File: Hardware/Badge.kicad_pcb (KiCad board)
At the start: 2 copper layers, 100 x 100 mm, 118 parts, among them J1 Battery_Conn, J2 Conn_01x02, J3 DEBUG, J4 Conn_02x15_Counter_Clockwise, J5 Conn_01x12, P1 USB_C_Plug_USB2.0, Q1 SI1967DH-T1-GE3, Q2 2SC4213, SW1 BOOT_MODE, SW2 RESET, SW3 PWR_BATT, SW4 SEL_BATT, SW5 Button B, SW6 Button A, U1 W25Q128JVS, U2 MCP73832-2-OT, U3 LD1117S33TR_SOT223, U4 RP2040, U5 BHI160B, U6 BMM150, U7 ESP32-S3-WROOM-1, X1 Simple_Addon_v2, Y1 12MHz_GND24

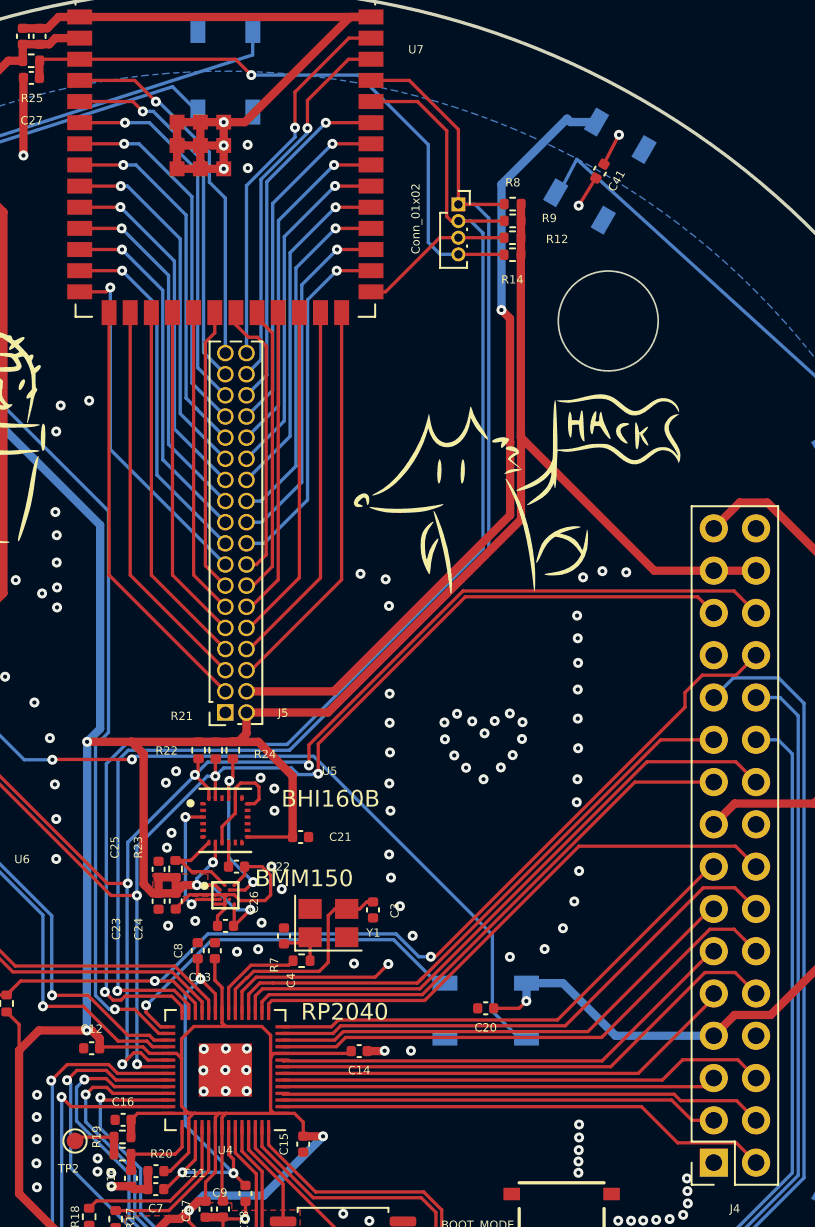
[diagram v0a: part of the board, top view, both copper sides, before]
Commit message: Inverted TX/RX from ESP32 - added INT line from BHI - Changed ESP32 dbg port to bigger footprint
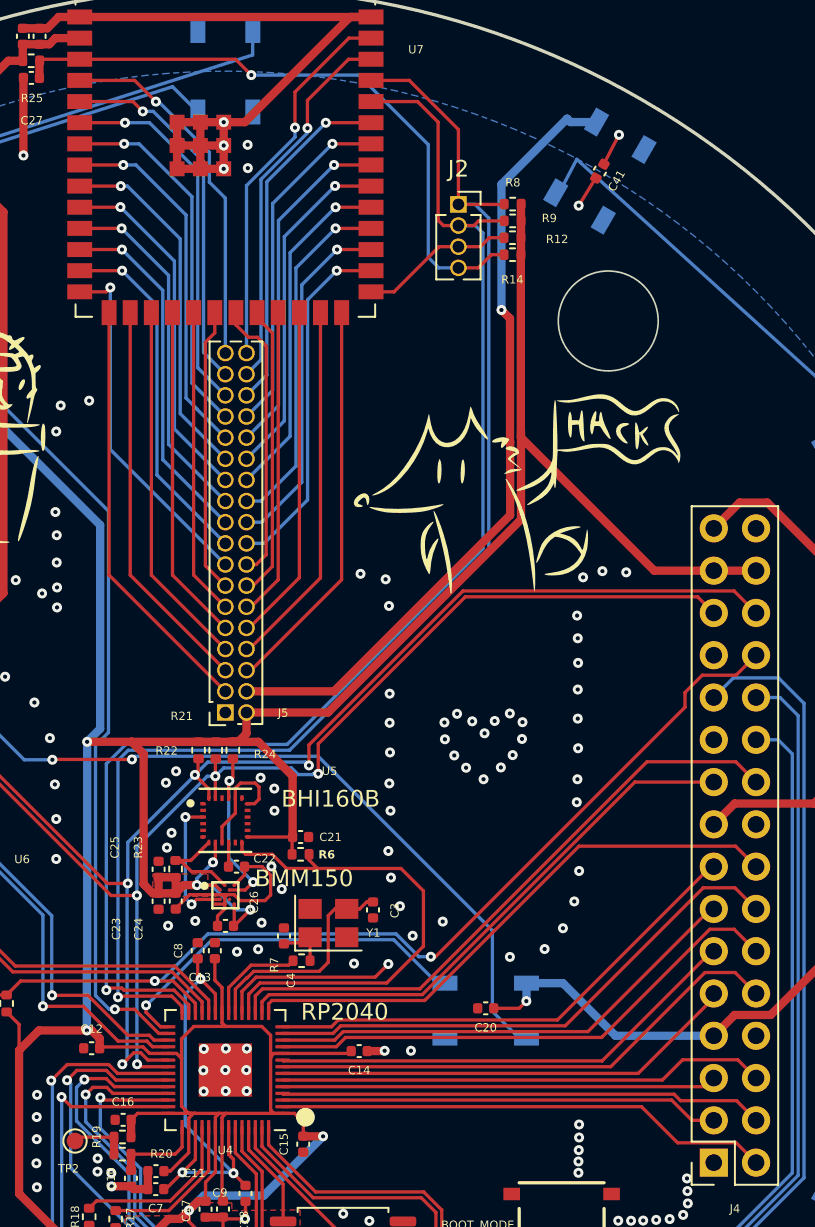
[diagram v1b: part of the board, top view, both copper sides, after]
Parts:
- added R6: 4.7k, Resistor_SMD:R_0402_1005Metric, F.Cu at (104.5, 102.0)
- J2: footprint Connector_PinSocket_1.00mm:PinSocket_1x04_P1.00mm_Vertical -> Connector_PinSocket_1.27mm:PinSocket_1x04_P1.27mm_Vertical
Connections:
- J4 pad 21: /GPIO_15 -> unconnected-(J4-Pin_21-Pad21)
- U4 pad 18: /GPIO_15 -> /INT
- U4 pad 27: /ESP_TX -> /ESP_RX
- U4 pad 28: /ESP_RX -> /ESP_TX
- U5 pad 12: /Gyros/INT -> /INT
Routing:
- net /GPIO_15: track 35.7 -> 0.00 mm
- net /INT: track 0.00 -> 29.6 mm
- net /ESP_EN: track 37.3 -> 38.5 mm
- net +3V3: track 317.6 -> 318.7 mm
- net /ESP_RX: track 82.0 -> 82.8 mm
- net GND: vias 190 -> 191

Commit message: First modification for v2
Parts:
- removed BT1: Battery_Cell, Battery:BatteryHolder_LINX_BAT-HLD-012-SMT
- removed D16: D_Schottky, Diode_SMD:D_SMA
- removed J2: Conn_01x02, Connector_PinSocket_1.27mm:PinSocket_1x04_P1.27mm_Vertical
- removed R22: 4.7k, Resistor_SMD:R_0402_1005Metric
- added C48: NC, Capacitor_SMD:C_0402_1005Metric, F.Cu at (67.6, 127.5)
- added C49: NC, Capacitor_SMD:C_0402_1005Metric, F.Cu at (67.6, 129.5)
- added C50: NC, Capacitor_SMD:C_0402_1005Metric, F.Cu at (67.6, 131.5)
- added C51: 10nF, Capacitor_SMD:C_0402_1005Metric, F.Cu at (82.7, 120.7)
- added D17: D, Diode_SMD:D_SOD-123F, F.Cu at (74.8, 125.4)
- added IC2: ST25DV04K-IER6S3, ST25DV:SOIC127P600X175-8N, F.Cu at (82.5, 124.9)
- added J6: Internal_I2C, Connector_PinHeader_1.00mm:PinHeader_1x03_P1.00mm_Vertical, F.Cu at (111.8, 97.6)
- added P2: ESP_DATA, Connector_USB:USB_C_Receptacle_Palconn_UTC16-G, F.Cu at (67.6, 70.5)
- added R29: 10k, Resistor_SMD:R_0402_1005Metric, F.Cu at (141.3, 62.3)
- added R30: 10k, Resistor_SMD:R_0402_1005Metric, F.Cu at (141.3, 64.3)
- added SW7: ESP_RST, TS-1184:TS-1187A-B-A-B, F.Cu at (130.1, 73.2)
- J3: footprint Connector_PinSocket_2.54mm:PinSocket_1x03_P2.54mm_Vertical -> Connector_PinHeader_1.27mm:PinHeader_1x03_P1.27mm_Vertical
- R12, R8, R9: value 10k -> 4.7k
- R21: value 4.7k -> 10k
- SW4: value SEL_BATT -> ESP_BOOT; footprint Button_Switch_SMD:SW_SPDT_CK-JS102011SAQN -> TS-1184:TS-1187A-B-A-B
- moved SW4 86.8 mm to (130.0, 66.2), turned to 0 degrees
- moved J1 40.8 mm to (88.7, 133.4)
- moved R12 19.3 mm to (135.4, 58.3)
- moved R14 19.3 mm to (135.4, 59.3)
- moved R9 19.3 mm to (135.4, 57.3)
- moved R8 19.3 mm to (135.4, 56.3)
- moved J3 7.20 mm to (85.4, 106.0)
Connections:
- net Net-(U5-ASCK) renamed /Gyros/INT_SCK
- net Net-(U5-ASDA) renamed /Gyros/INT_SDA
- J5 pad 15: /WiFi_BT/IO43 -> unconnected-(J5-Pin_15-Pad15)
- J5 pad 17: /WiFi_BT/IO44 -> unconnected-(J5-Pin_17-Pad17)
- R12 pad 1: /ESP_BOOT -> +3V3
- R12 pad 2: +3V3 -> /I2C_SCL
- R14 pad 1: /ESP_EN -> /ESP_RX
- R21 pad 1: +3V3 -> /ESP_TX
- R21 pad 2: /I2C_SCL -> +3V3
- R6 pad 2: /INT -> /NFC_INT
- R8 pad 1: /ESP_TX -> +3V3
- R8 pad 2: +3V3 -> /I2C_SDA
- R9 pad 1: /ESP_RX -> +3V3
- R9 pad 2: +3V3 -> /SEN_INT
- SW3 pad 1: Net-(D16-K) -> Net-(J1-Pin_2)
- SW4 pad 1: Net-(J1-Pin_2) -> GND
- SW4 pad 2: Net-(D16-A) -> /WiFi_BT/ESP_BOOT
- U2 pad 3: Net-(D16-K) -> Net-(J1-Pin_2)
- U4 pad 17: /GPIO_14 -> /NFC_INT
- U4 pad 18: /INT -> /SEN_INT
- U5 pad 12: /INT -> /SEN_INT
- U7 pad 13: /WiFi_BT/IO44 -> /WiFi_BT/ESP_USB-
- U7 pad 14: /WiFi_BT/IO43 -> /WiFi_BT/ESP_USB+
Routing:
- net (no net): track 0.00 -> 72.7 mm, vias 0 -> 2
- net Net-(D16-K): track 48.4 -> 0.00 mm
- net Net-(BT1-+): track 36.7 -> 0.00 mm
- net /INT: track 29.6 -> 0.00 mm
- net /WiFi_BT/IO44: track 21.6 -> 0.00 mm, vias 1 -> 0
- net /WiFi_BT/IO43: track 21.5 -> 0.00 mm, vias 1 -> 0
- net /ESP_RX: track 82.8 -> 72.6 mm
- net /ESP_TX: track 82.1 -> 74.9 mm
- net /SWCLK: track 22.5 -> 15.8 mm
- net /SWD: track 21.0 -> 14.8 mm
- net Net-(D16-A): track 4.22 -> 0.00 mm
- net /ESP_BOOT: track 9.34 -> 5.21 mm
- net /ESP_EN: track 38.5 -> 35.4 mm
- net Net-(J1-Pin_2): track 8.89 -> 10.7 mm

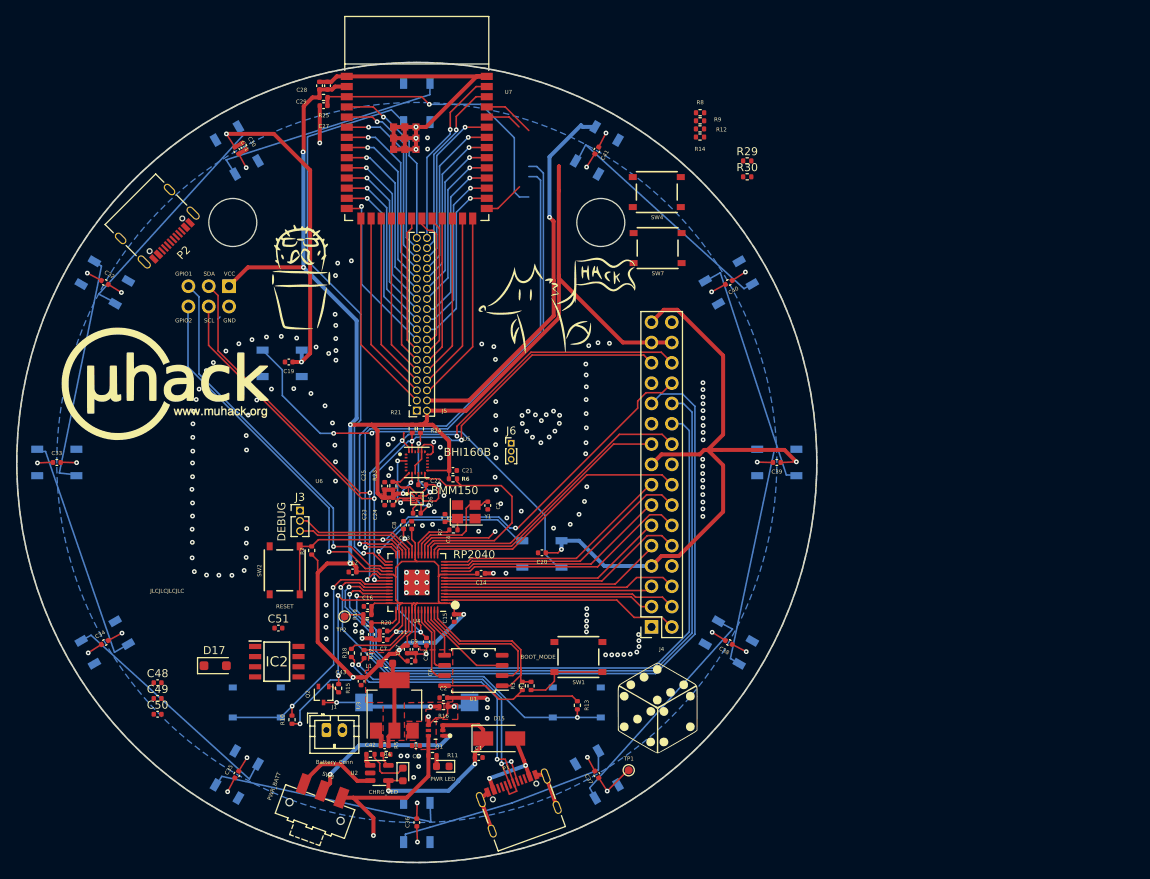
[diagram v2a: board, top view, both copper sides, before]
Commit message: WIP - Added NFC Antenna and connected almost everythings else
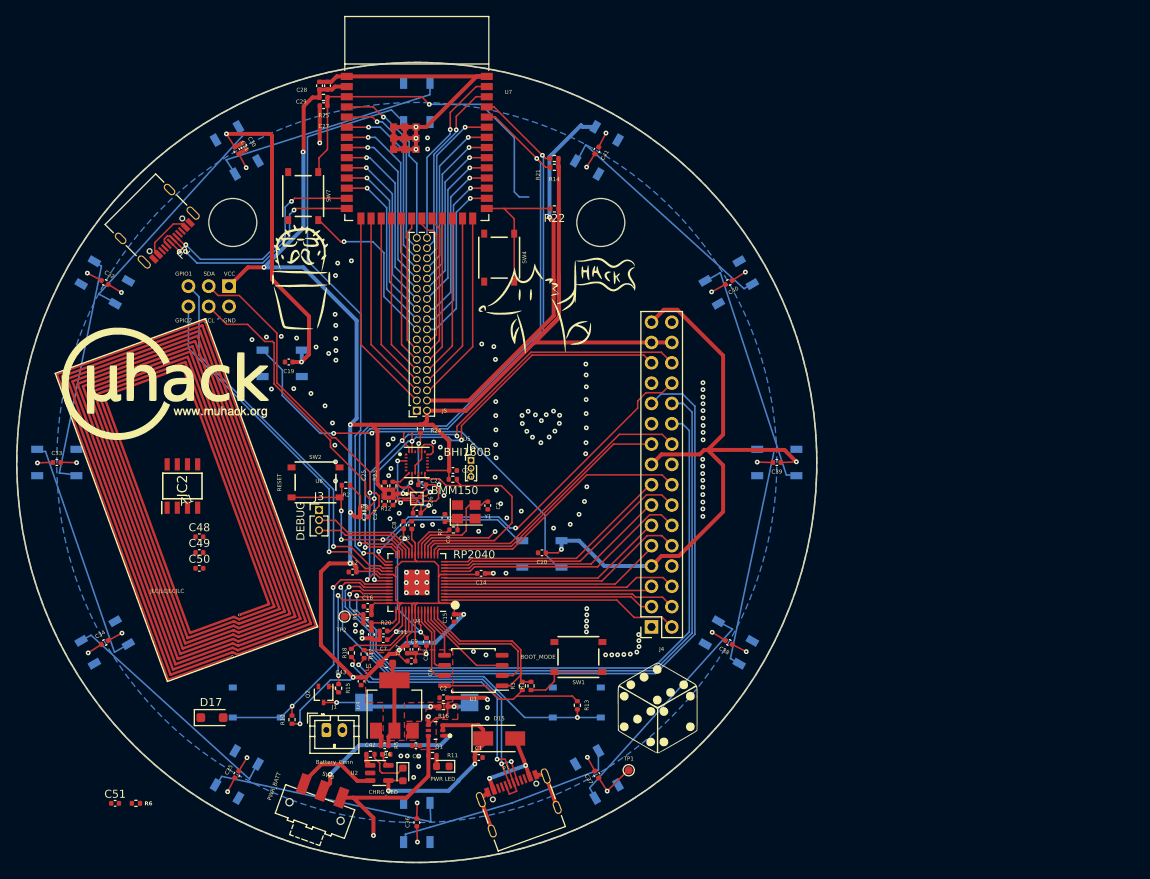
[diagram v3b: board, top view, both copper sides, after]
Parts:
- removed R29, R30: 10k, Resistor_SMD:R_0402_1005Metric
- added A1: MuTag_NFC_Antenna, MuHack Badge NFC Antenna:muhack_badge_antenna, F.Cu at (54.8, 88.9)
- added R22: 10k, Resistor_SMD:R_0402_1005Metric, F.Cu at (117.2, 68.3)
- moved R8 65.7 mm to (93.4, 106.8)
- moved R12 63.3 mm to (93.5, 105.7)
- moved R6 56.7 mm to (64.9, 142.6)
- moved R9 54.4 mm to (104.5, 102.1)
- moved SW7 44.8 mm to (85.8, 66.7), turned to 90 degrees
- moved R21 38.2 mm to (117.2, 62.0), turned to 0 degrees
- moved C51 29.9 mm to (62.3, 142.6)
- moved IC2 24.9 mm to (70.7, 102.9), turned to 90 degrees
- moved SW4 21.3 mm to (110.3, 74.4), turned to 90 degrees
- moved C48 19.0 mm to (72.8, 109.3)
- moved C49 19.0 mm to (72.8, 111.3)
- moved C50 19.0 mm to (72.8, 113.2)
- moved R14 18.6 mm to (117.2, 63.1)
- moved SW2 11.6 mm to (87.3, 102.5), turned to 180 degrees
- moved R2 9.20 mm to (91.1, 102.8), turned to 0 degrees
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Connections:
- J5 pad 15: unconnected-(J5-Pin_15-Pad15) -> /ESP_BOOT
- J5 pad 17: unconnected-(J5-Pin_17-Pad17) -> /ESP_EN
- SW4 pad 2: /WiFi_BT/ESP_BOOT -> /ESP_BOOT
- SW7 pad 2: /WiFi_BT/ESP_EN -> /ESP_EN
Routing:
- net (no net): track 72.7 -> 0.00 mm, vias 2 -> 0
- net /WiFi_BT/ESP_USB-: track 0.00 -> 30.6 mm, vias 0 -> 3
- net /ESP_EN: track 35.4 -> 65.6 mm, vias 1 -> 2
- net /WiFi_BT/ESP_USB+: track 0.00 -> 29.7 mm, vias 0 -> 2
- net /SEN_INT: track 0.00 -> 29.6 mm
- net +3V3: track 318.7 -> 333.5 mm, vias 11 -> 12
- net /ESP_BOOT: track 5.21 -> 17.7 mm
- net /ESP_RX: track 72.6 -> 79.9 mm, vias 1 -> 2
- net Net-(P2-VBUS-PadA4): track 0.00 -> 6.65 mm
- net /I2C_SDA: track 99.8 -> 105.4 mm
- net /ESP_TX: track 74.9 -> 79.1 mm, vias 1 -> 2
- net /I2C_SCL: track 93.5 -> 96.5 mm
- net /SWD: track 14.8 -> 12.5 mm
- net /SWCLK: track 15.8 -> 13.5 mm
- net /RUN: track 66.2 -> 67.7 mm, vias 2 -> 4
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
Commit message: All upgrade done, start working on lesser stuff (like silkscreen)
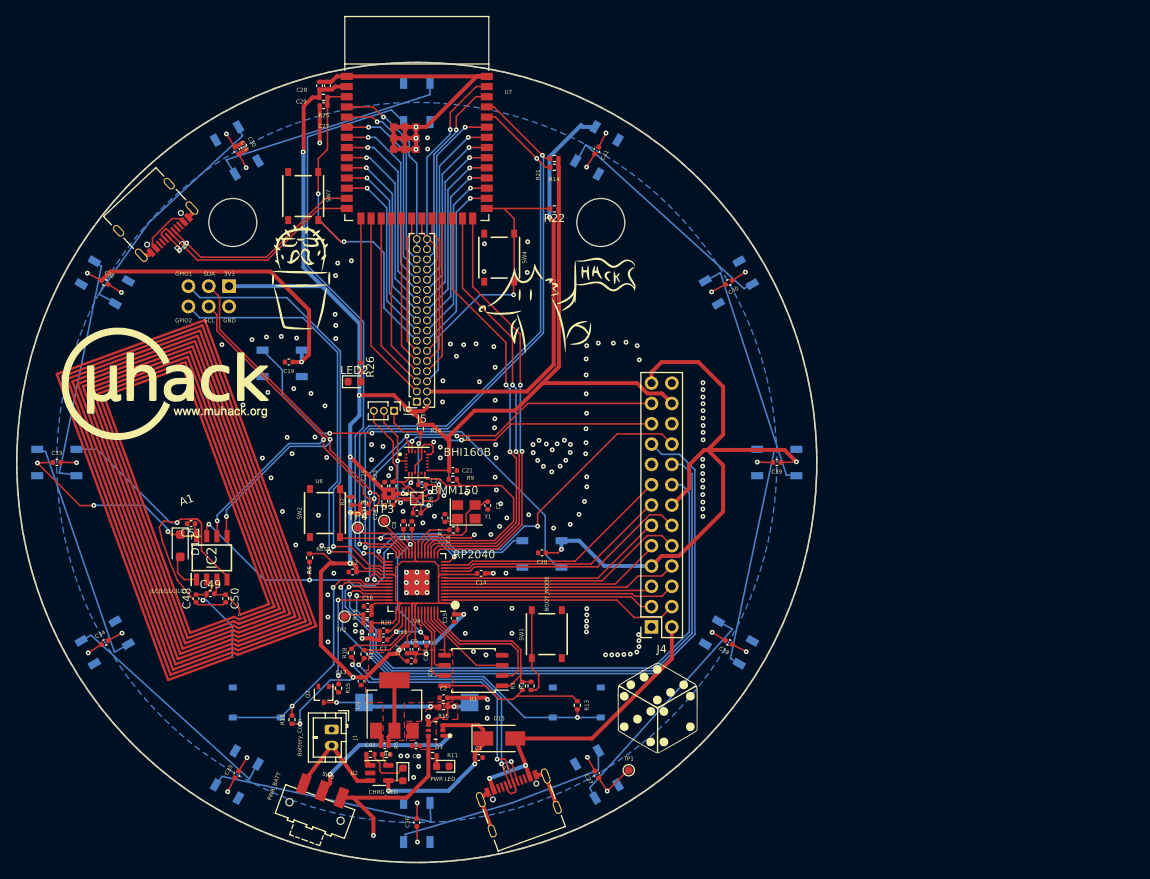
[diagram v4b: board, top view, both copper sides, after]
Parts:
- removed J3: DEBUG, Connector_PinHeader_1.27mm:PinHeader_1x03_P1.27mm_Vertical
- removed L1: 330H-1.7A, Inductor_SMD:L_0603_1608Metric
- added LED2: ESP LED, LED_SMD:LED_0603_1608Metric, F.Cu at (92.2, 89.9)
- added R26: 470, Resistor_SMD:R_0402_1005Metric, F.Cu at (93.0, 88.0)
- added TP3: TestPoint, TestPoint:TestPoint_Pad_D1.0mm, F.Cu at (95.9, 107.3)
- added TP4: TestPoint, TestPoint:TestPoint_Pad_D1.0mm, F.Cu at (92.6, 108.2)
- J4: footprint Connector_PinSocket_2.54mm:PinSocket_2x16_P2.54mm_Vertical -> Connector_PinSocket_2.54mm:PinSocket_2x13_P2.54mm_Vertical
- J5: footprint Connector_PinSocket_1.27mm:PinSocket_2x18_P1.27mm_Vertical -> Connector_PinSocket_1.27mm:PinSocket_2x17_P1.27mm_Vertical
- J6: footprint Connector_PinHeader_1.00mm:PinHeader_1x03_P1.00mm_Vertical -> Connector_PinHeader_1.27mm:PinHeader_1x03_P1.27mm_Vertical
- moved R6 37.6 mm to (86.6, 111.9), turned to -90 degrees
- moved C51 36.2 mm to (71.8, 107.6), turned to 180 degrees
- moved D17 21.9 mm to (70.4, 110.4), turned to -90 degrees
- moved J6 11.4 mm to (97.2, 93.5), turned to -90 degrees
- moved IC2 9.70 mm to (74.4, 111.9)
- moved C48 7.72 mm to (72.4, 117.0), turned to 90 degrees
- moved C49 5.32 mm to (74.2, 116.4)
- moved C50 5.00 mm to (76.1, 117.0), turned to -90 degrees
- moved SW1 4.88 mm to (116.2, 121.5), turned to -90 degrees
- moved SW2 4.01 mm to (88.5, 106.3), turned to -90 degrees
- moved R2 2.12 mm to (91.9, 104.8), turned to -90 degrees
- moved J5 1.12 mm to (100.0, 92.4)
- moved P2 0.82 mm to (67.4, 69.7), turned to -137 degrees
- moved J1 0.66 mm to (89.4, 133.4), turned to -90 degrees
- moved R8 0.48 mm to (93.5, 106.3)
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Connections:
- net /ADC_3 renamed /ADC_BUZZ
- C42 pad 2: Net-(U3-VO) -> +3V3
- J4 pad 14: /GPIO_10 -> VCC
- J4 pad 15: /GPIO_11 -> /GPIO_10
- J4 pad 16: /GPIO_12 -> /ADC_2
- J4 pad 17: VCC -> GND
- J4 pad 18: GND -> /ADC_1
- J4 pad 19: /GPIO_13 -> /ADC_0
- J4 pad 2: /GPIO_0 -> VBUS
- J4 pad 20: /GPIO_14 -> /RUN
- J4 pad 21: unconnected-(J4-Pin_21-Pad21) -> /I2C_SCL
- J4 pad 22: /ADC_2 -> GND
- J4 pad 23: /ADC_0 -> /I2C_SDA
- J4 pad 24: /ADC_1 -> +3V3
- J4 pad 25: GND -> VCC
- J4 pad 26: /RUN -> GND
- J4 pad 4: /GPIO_2 -> /GPIO_0
- J4 pad 6: /GPIO_4 -> /GPIO_2
- J4 pad 8: GND -> /GPIO_4
- J5 pad 10: /WiFi_BT/IO47 -> /WiFi_BT/IO14
- J5 pad 11: /WiFi_BT/IO11 -> /WiFi_BT/IO12
- J5 pad 12: /WiFi_BT/IO21 -> /WiFi_BT/IO13
- J5 pad 13: /WiFi_BT/IO12 -> /ESP_EN
- J5 pad 14: /WiFi_BT/IO14 -> /WiFi_BT/IO35
- J5 pad 15: /ESP_BOOT -> /WiFi_BT/IO8
- J5 pad 16: /WiFi_BT/IO13 -> /WiFi_BT/IO36
- J5 pad 17: /ESP_EN -> /WiFi_BT/IO18
- J5 pad 18: /WiFi_BT/IO35 -> /WiFi_BT/IO37
- J5 pad 19: /WiFi_BT/IO8 -> /WiFi_BT/IO17
- J5 pad 20: /WiFi_BT/IO36 -> /WiFi_BT/IO38
- J5 pad 21: /WiFi_BT/IO18 -> /WiFi_BT/IO16
- J5 pad 22: /WiFi_BT/IO37 -> /WiFi_BT/IO39
- J5 pad 23: /WiFi_BT/IO17 -> /WiFi_BT/IO15
- J5 pad 24: /WiFi_BT/IO38 -> /WiFi_BT/IO40
- J5 pad 25: /WiFi_BT/IO16 -> /WiFi_BT/IO7
- J5 pad 26: /WiFi_BT/IO39 -> /WiFi_BT/IO41
- J5 pad 27: /WiFi_BT/IO15 -> /WiFi_BT/IO6
- J5 pad 28: /WiFi_BT/IO40 -> /WiFi_BT/IO42
- J5 pad 29: /WiFi_BT/IO7 -> /WiFi_BT/IO5
- J5 pad 3: /WiFi_BT/IO3 -> /WiFi_BT/IO46
- J5 pad 30: /WiFi_BT/IO41 -> /WiFi_BT/IO2
- J5 pad 31: /WiFi_BT/IO6 -> /WiFi_BT/IO4
- J5 pad 32: /WiFi_BT/IO42 -> /WiFi_BT/IO1
- J5 pad 33: /WiFi_BT/IO5 -> (no net)
- J5 pad 34: /WiFi_BT/IO2 -> (no net)
- J5 pad 5: /WiFi_BT/IO46 -> /WiFi_BT/IO9
- J5 pad 6: /WiFi_BT/IO45 -> /ESP_BOOT
- J5 pad 7: /WiFi_BT/IO9 -> /WiFi_BT/IO10
- J5 pad 8: /WiFi_BT/IO48 -> /WiFi_BT/IO21
- J5 pad 9: /WiFi_BT/IO10 -> /WiFi_BT/IO11
- J6 pad 2: /Gyros/INT_SCK -> /Gyros/INT_S1
- J6 pad 3: /Gyros/INT_S1 -> /Gyros/INT_SCK
- U3 pad 2: Net-(U3-VO) -> +3V3
- U4 pad 14: /GPIO_11 -> /NFC_INT
- U4 pad 15: /GPIO_12 -> /ESP_45
- U4 pad 16: /GPIO_13 -> /ESP_48
- U4 pad 17: /NFC_INT -> /ESP_47
- U7 pad 24: /WiFi_BT/IO47 -> /ESP_47
- U7 pad 25: /WiFi_BT/IO48 -> /ESP_48
- U7 pad 26: /WiFi_BT/IO45 -> /ESP_45
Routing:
- net /ESP_47: track 0.00 -> 54.3 mm, vias 0 -> 2
- net /ESP_48: track 0.00 -> 53.8 mm, vias 0 -> 2
- net /ESP_45: track 0.00 -> 53.2 mm, vias 0 -> 2
- net GND: track 135.4 -> 182.5 mm, vias 154 -> 183
- net /NFC_INT: track 0.00 -> 44.3 mm, vias 0 -> 3
- net /GPIO_14: track 37.4 -> 0.00 mm
- net /GPIO_12: track 34.3 -> 0.00 mm
- net /GPIO_13: track 33.3 -> 0.00 mm
- net /GPIO_11: track 29.9 -> 0.00 mm
- net VBUS: track 11.5 -> 39.2 mm
- net VCC: track 224.3 -> 249.7 mm, vias 17 -> 19
- net /WiFi_BT/IO45: track 24.0 -> 0.00 mm
- net /WiFi_BT/IO48: track 22.2 -> 0.00 mm
- net /ESP_EN: track 65.6 -> 45.2 mm
- net /WiFi_BT/IO47: track 20.3 -> 0.00 mm
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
